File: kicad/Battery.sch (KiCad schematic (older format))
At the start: 4 parts, among them J1 Balance conn, J3 Bat conn

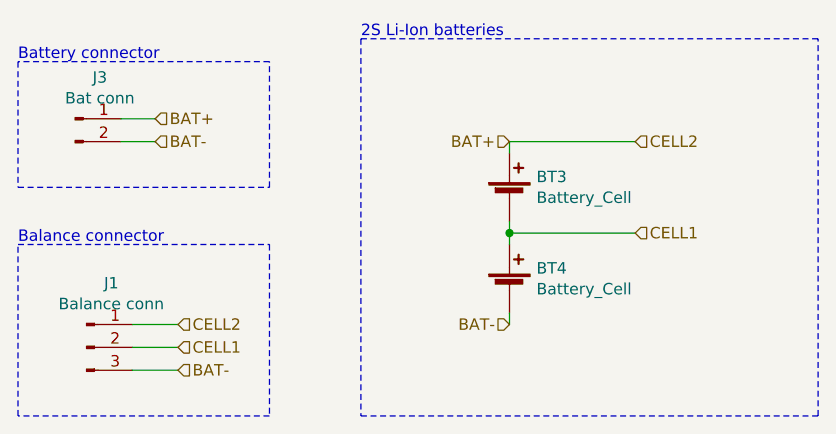
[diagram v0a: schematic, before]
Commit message: Updated schematic
Made some error with first rev, the found error are now corrected.
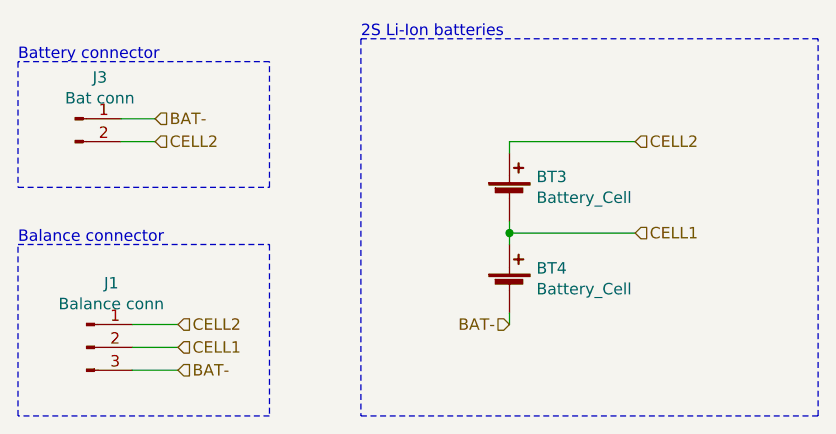
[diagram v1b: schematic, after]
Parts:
- J1: footprint (none) -> Connector_JST:JST_XH_B3B-XH-A_1x03_P2.50mm_Vertical
- J3: footprint Powerbank:XT30PW-M -> connectors:XT30PW-M
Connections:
- net BAT-: now also J3.1 (Pin_1); no longer J3.2 (Pin_2)
- net BAT+ renamed CELL2
- net CELL2: now also J3.2 (Pin_2); no longer J3.1 (Pin_1)
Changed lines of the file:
@@
 $Descr A4 11693 8268
 encoding utf-8
-Sheet 3 6
+Sheet 3 7
 Title "USB-C PD controller with 4S battery charger"
 Date "2020-01-11"
@@
 F 0 "J3" H 3858 3381 50  0000 C CNN
 F 1 "Bat conn" H 3858 3290 50  0000 C CNN
-F 2 "Powerbank:XT30PW-M" H 3750 3200 50  0001 C CNN
+F 2 "connectors:XT30PW-M" H 3750 3200 50  0001 C CNN
 F 3 "~" H 3750 3200 50  0001 C CNN
 	1    3750 3200
@@
 Text Notes 5000 2850 0    50   ~ 0
 2S Li-Ion batteries
-Text HLabel 5650 3300 0    50   Input ~ 0
-BAT+
 Text HLabel 5650 4100 0    50   Input ~ 0
 BAT-
@@
 F 0 "J1" H 3908 4481 50  0000 C CNN
 F 1 "Balance conn" H 3908 4390 50  0000 C CNN
-F 2 "" H 3800 4200 50  0001 C CNN
+F 2 "Connector_JST:JST_XH_B3B-XH-A_1x03_P2.50mm_Vertical" H 3800 4200 50  0001 C CNN
 F 3 "~" H 3800 4200 50  0001 C CNN
 	1    3800 4200
@@
 Text HLabel 4200 4100 2    50   Input ~ 0
 CELL2
+Text HLabel 4100 3200 2    50   Input ~ 0
+BAT-
 Text HLabel 4100 3300 2    50   Input ~ 0
-BAT-
-Text HLabel 4100 3200 2    50   Input ~ 0
-BAT+
+CELL2
 $EndSCHEMATC
